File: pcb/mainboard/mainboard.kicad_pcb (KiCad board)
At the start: 10 copper layers, 165 x 121 mm, 629 parts, among them J1 CONN_PCIE_PWR_8PIN, J10 FAN_01, J11 XILINX_JTAG, J12 JUMPER_0402_SPDT, J13 JUMPER_0402_SPDT, J14 RJ45, J15 PMOD_HOST, J16 SMPM, J17 SMPM, J18 SMPM, J19 SMPM, J2 CONN_IBC_MGMT, J20 SMPM, J21 SMPM, J22 SMPM, J23 SMPM, J24 SMPM, J25 SMPM, J26 SMPM, J27 0826-1G1T-23-F, J28 SMPM, J29 SMPM, J3 CONN_01X03, J30 SMPM, J31 SMPM, J32 SMPM, J33 SMPM, J34 SMPM, J35 SMPM, J36 SMPM, J37 SMPM, J38 SMPM, J39 SMPM, J4 CONN_01X05, J40 SMPM, J41 SMPM, J42 SMPM, J43 SMPM, J44 SMPM, J45 SMPM, J46 SMPM, J47 SMPM, J48 CONN_01X10, J5 XILINX_JTAG, J6 CONN_SFP_HOST, J7 SFP_CAGE, J8 FAN_01, J9 CONN_01X03, K1 RELAY_TE_HF3_96, K2 RELAY_TE_HF3_96, K3 RELAY_TE_HF3_96, K4 RELAY_TE_HF3_96, M1 960-23-23-F-AB-0, SW1 SWITCH, SW2 SWITCH, U1 STM32L031C6U6, U10 MAX40026, U11 MAX40026, U12 MAX40026, U13 MAX40026, U14 MAX40026, U15 MAX40026, U16 MAX40026, U17 MAX40026, U18 MAX40026, U19 MAX40026, U2 MYMGK1R812ERSR, U20 MAX40026, U21 DAC60508, U22 DAC60508, U23 STM32H735-UFBGA176-25, U24 AT24MAC402, U25 ADM3101E_QFN, U26 LMR70503, U27 SIT9121AI-2BF-XXS200.000000G, U28 SIT9121AI-2BF-XXS156.250000G, U29 HMC675LP3E, U3 MYMGK00504ERSR, U30 SIT9121AI-2BF-XXS200.000000G, U31 ECS-1612MV-250-CN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

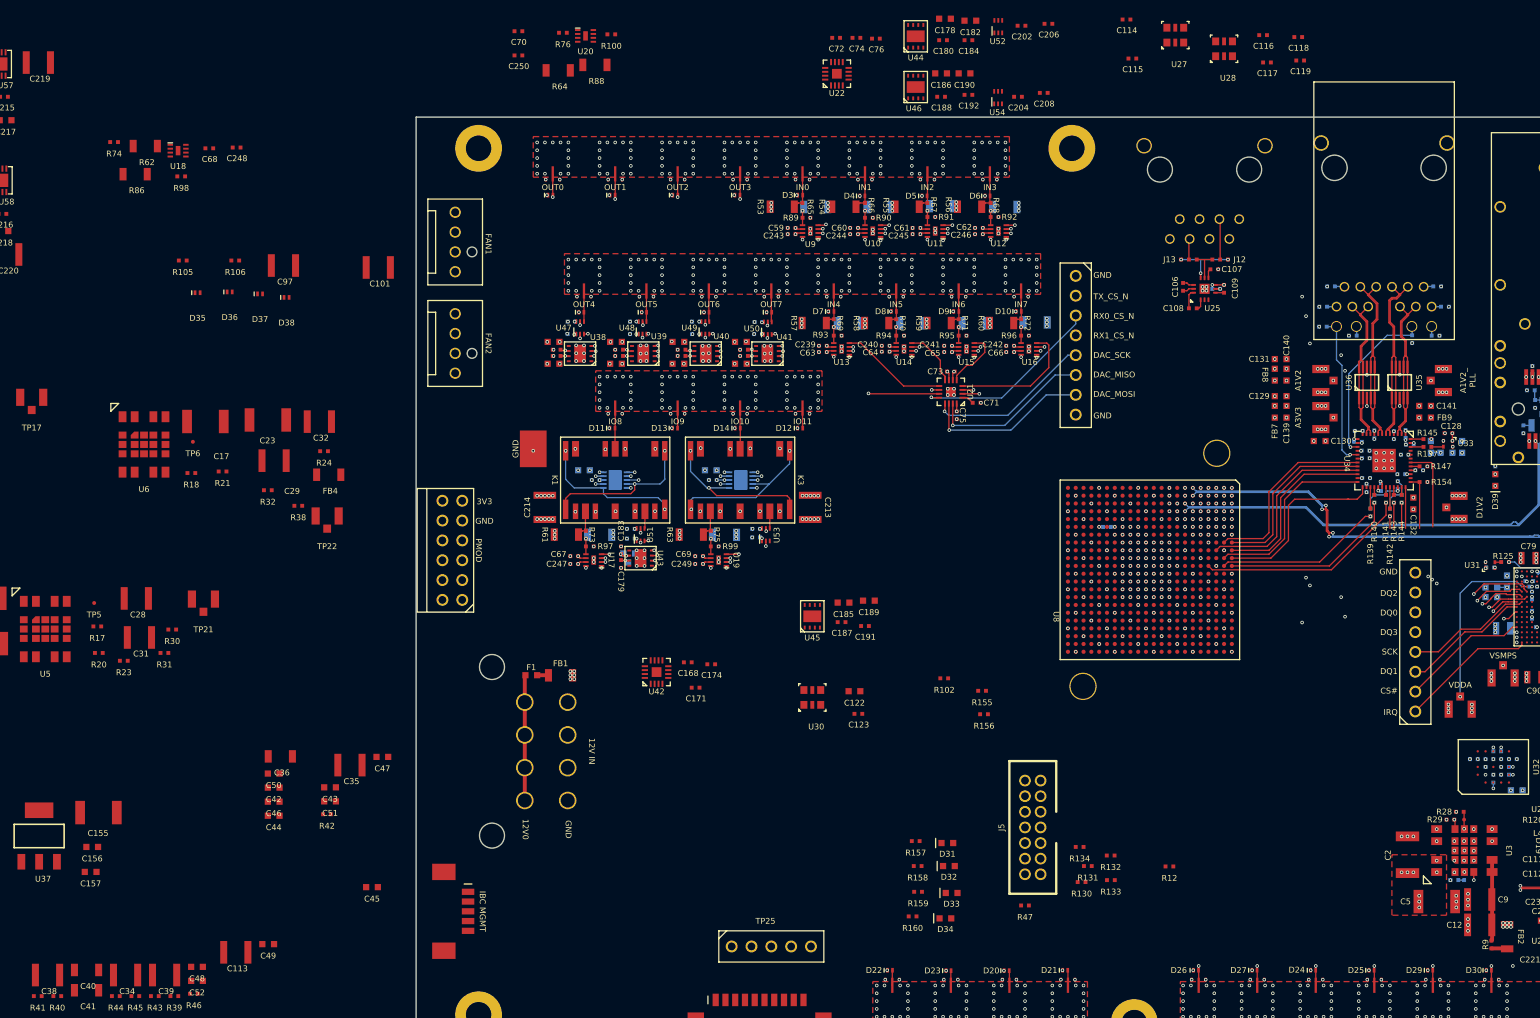
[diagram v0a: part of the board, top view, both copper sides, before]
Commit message: Hooked up most input pins
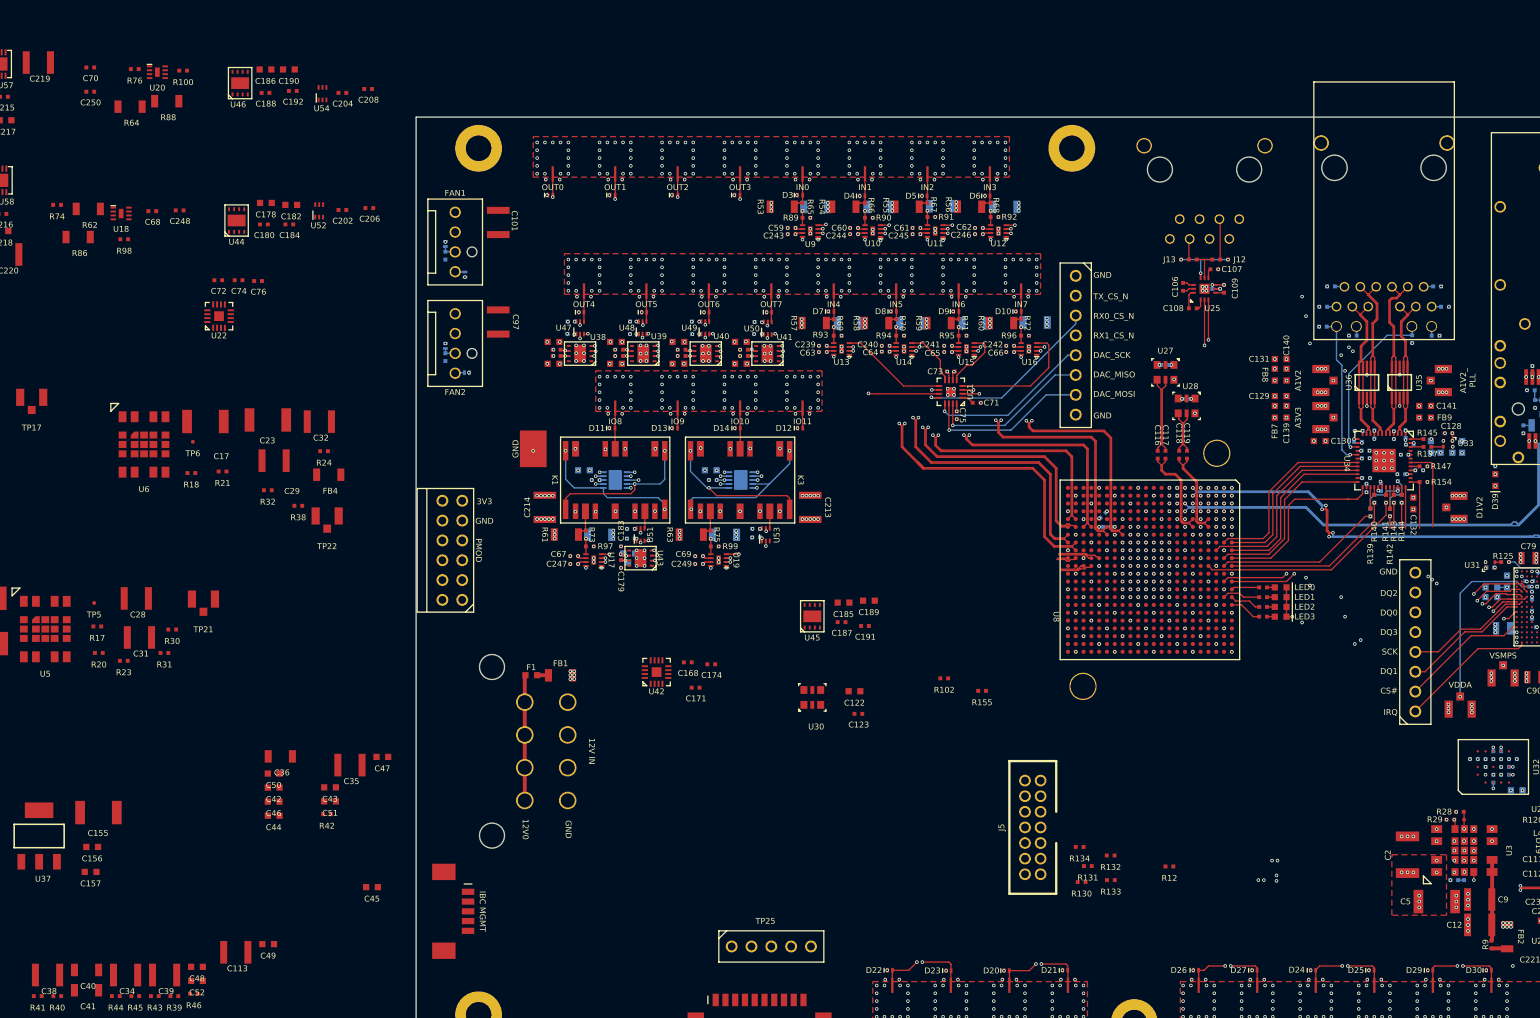
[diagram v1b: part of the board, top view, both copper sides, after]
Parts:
- C114, C115, D35, D36, D37, D38, R105, R106, R156, R47: moved to B.Cu
- moved C202 90.1 mm to (105.5, 31.9)
- moved C178 90.1 mm to (95.8, 31.0)
- moved C180 90.1 mm to (95.5, 33.8)
- moved C182 90.1 mm to (99.0, 31.2)
- moved C184 90.1 mm to (98.8, 33.8)
- moved C206 90.1 mm to (109.0, 31.6)
- moved U44 90.1 mm to (92.0, 33.2)
- moved U52 90.1 mm to (102.6, 32.0)
- moved C208 86.6 mm to (108.8, 16.4)
- moved U54 86.6 mm to (103.0, 17.0)
- moved C186 86.6 mm to (95.7, 13.9)
- moved C188 86.6 mm to (95.7, 16.9)
- moved C190 86.6 mm to (98.7, 13.9)
- moved C192 86.6 mm to (99.2, 16.6)
- moved C204 86.6 mm to (105.5, 16.9)
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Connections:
- R157 pad 1: /Management/FPGA_LED0 -> /FPGA Support/FPGA_LED0
- R158 pad 1: /Management/FPGA_LED1 -> /FPGA Support/FPGA_LED1
- R159 pad 1: /Management/FPGA_LED2 -> /FPGA Support/FPGA_LED2
- R160 pad 1: /Management/FPGA_LED3 -> /FPGA Support/FPGA_LED3
- R163 pad 1: /Management/SFP_LED1 -> /FPGA Support/SFP_LED1
- R164 pad 1: /Management/SFP_LED2 -> /FPGA Support/SFP_LED2
- U8 pad A13: unconnected-(U8-PadA13) -> /FPGA Support/SFP_LED1
- U8 pad A14: unconnected-(U8-PadA14) -> /FPGA Support/FPGA_LED0
- U8 pad A15: unconnected-(U8-PadA15) -> /FPGA Support/FPGA_LED2
- U8 pad A16: unconnected-(U8-PadA16) -> /FPGA Support/FPGA_LED3
- U8 pad A3: /Transceivers/BERT_TX1_N -> /Transceivers/BERT_TX0_N
- U8 pad A4: /Transceivers/BERT_TX1_P -> /Transceivers/BERT_TX0_P
- U8 pad AA10: /Inputs/TRIGIN_3_P -> /Inputs/TRIGIN_9_P
- U8 pad AA5: /Inputs/TRIGIN_0_P -> /Inputs/TRIGIN_2_N
- U8 pad AA6: /Inputs/TRIGIN_2_P -> /Inputs/TRIGIN_5_N
- U8 pad AB10: /Inputs/TRIGIN_3_N -> /Inputs/TRIGIN_9_N
- U8 pad AB5: /Inputs/TRIGIN_0_N -> /Inputs/TRIGIN_2_P
- U8 pad AB6: /Inputs/TRIGIN_2_N -> /Inputs/TRIGIN_5_P
- U8 pad B1: /Transceivers/BERT_TX0_N -> /Transceivers/BERT_TX1_N
- U8 pad B13: unconnected-(U8-PadB13) -> /FPGA Support/SFP_LED2
- U8 pad B15: unconnected-(U8-PadB15) -> /FPGA Support/FPGA_LED1
- U8 pad B2: /Transceivers/BERT_TX0_P -> /Transceivers/BERT_TX1_P
- U8 pad B5: /Transceivers/BERT_RX1_N -> /Transceivers/BERT_RX0_N
- U8 pad B6: /Transceivers/BERT_RX1_P -> /Transceivers/BERT_RX0_P
- U8 pad C3: /Transceivers/BERT_RX0_N -> /Transceivers/BERT_RX1_N
- U8 pad C4: /Transceivers/BERT_RX0_P -> /Transceivers/BERT_RX1_P
- U8 pad F20: /Management/FPGA_LED1 -> unconnected-(U8-PadF20)
- U8 pad G20: /Management/FPGA_LED0 -> unconnected-(U8-PadG20)
- U8 pad K19: /Management/FPGA_LED3 -> unconnected-(U8-PadK19)
- U8 pad L18: /Management/FPGA_LED2 -> unconnected-(U8-PadL18)
- U8 pad L19: /Management/SFP_LED1 -> unconnected-(U8-PadL19)
- U8 pad L20: /Management/SFP_LED2 -> unconnected-(U8-PadL20)
- U8 pad U6: /Inputs/TRIGIN_9_N -> /Inputs/TRIGIN_3_N
- U8 pad U7: /Inputs/TRIGIN_9_P -> /Inputs/TRIGIN_3_P
- U8 pad W11: /Inputs/TRIGIN_5_P -> /Inputs/TRIGIN_0_P
- U8 pad W6: /Inputs/TRIGIN_6_P -> /Inputs/TRIGIN_6_N
- U8 pad Y11: /Inputs/TRIGIN_5_N -> /Inputs/TRIGIN_0_N
- U8 pad Y6: /Inputs/TRIGIN_6_N -> /Inputs/TRIGIN_6_P
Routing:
- net /Transceivers/BERT_TX0_N: track 1.90 -> 109.7 mm, vias 1 -> 3
- net /Transceivers/BERT_TX0_P: track 1.95 -> 108.4 mm, vias 1 -> 3
- net /Transceivers/BERT_TX1_N: track 1.95 -> 101.0 mm, vias 1 -> 3
- net /Transceivers/BERT_TX1_P: track 1.90 -> 100.3 mm, vias 1 -> 3
- net /Transceivers/FASTSYNC_TX_N: track 2.47 -> 95.2 mm
- net /Transceivers/FASTSYNC_TX_P: track 2.49 -> 95.2 mm
- net /Transceivers/BERT_RX1_N: track 2.51 -> 76.5 mm
- net /Transceivers/BERT_RX1_P: track 2.50 -> 76.2 mm
- net /Management/MCU_UART_RX: track 25.6 -> 93.4 mm, vias 1 -> 4
- net /Management/MCU_UART_TX: track 26.5 -> 93.8 mm, vias 1 -> 4
- net /Transceivers/BERT_RX0_P: track 2.51 -> 66.2 mm
- net /Transceivers/BERT_RX0_N: track 2.61 -> 66.3 mm
- net /GND: track 1866.9 -> 1924.6 mm, vias 1149 -> 1156
- net /Transceivers/CDRTRIG_RX_N: track 43.4 -> 99.3 mm, vias 2 -> 3
- net /Transceivers/CDRTRIG_RX_P: track 43.2 -> 99.0 mm, vias 2 -> 3
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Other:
- board text removed: "FPGA LEDs"
- board text removed: "GTX clocks"

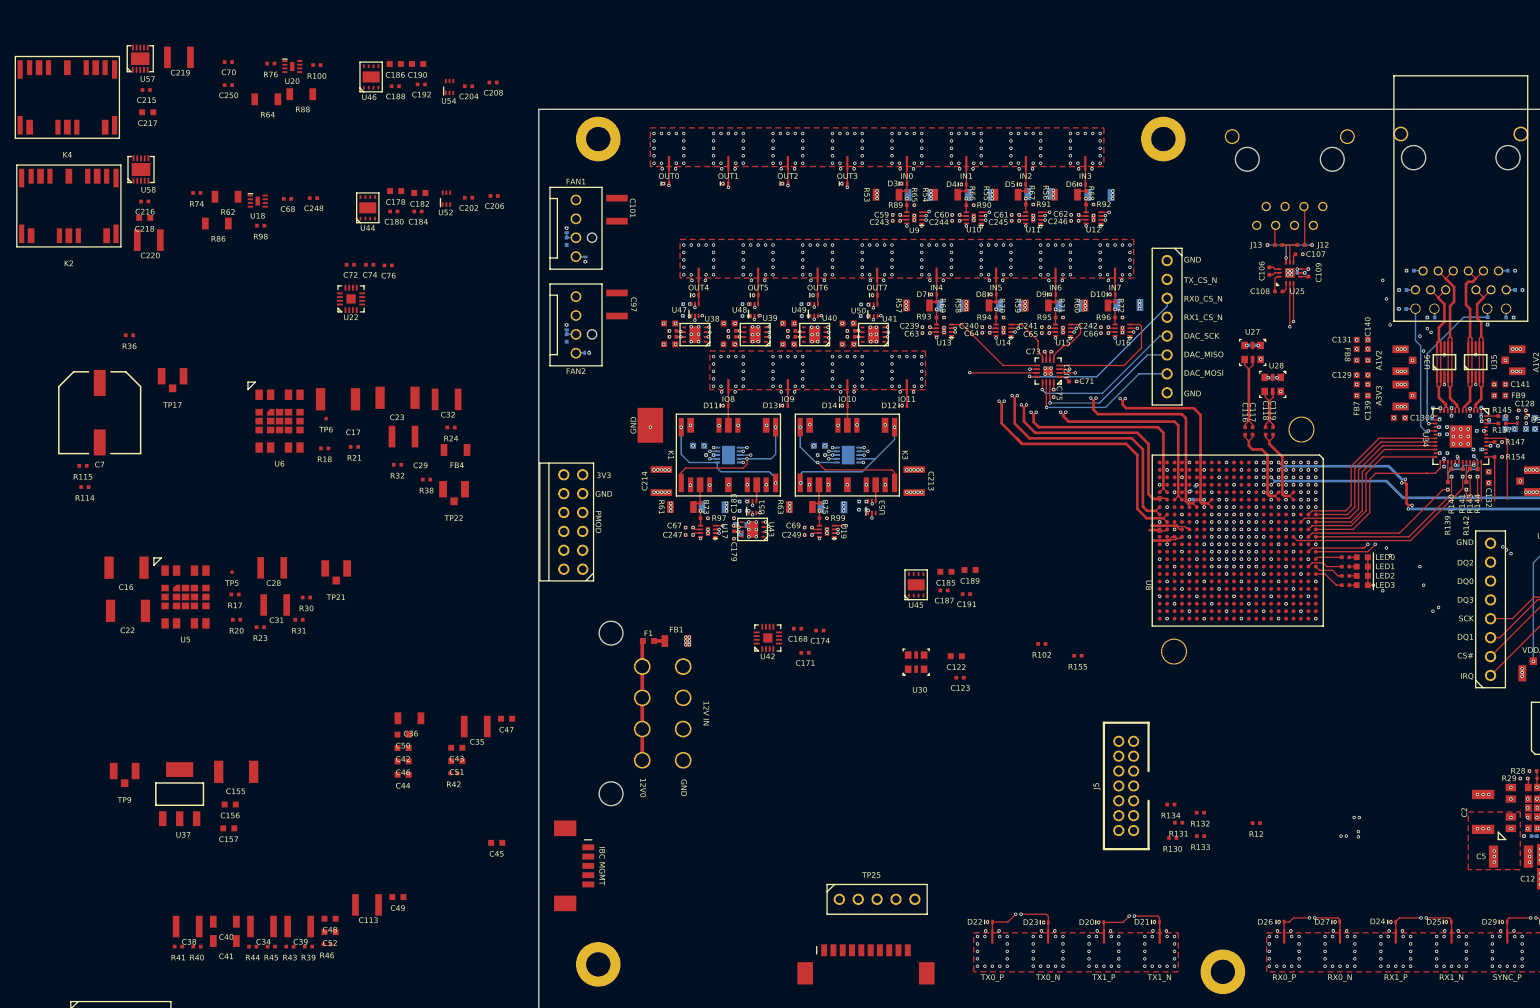
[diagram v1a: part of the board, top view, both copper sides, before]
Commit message: Hooked up PMOD, initial placement of FPGA JTAG
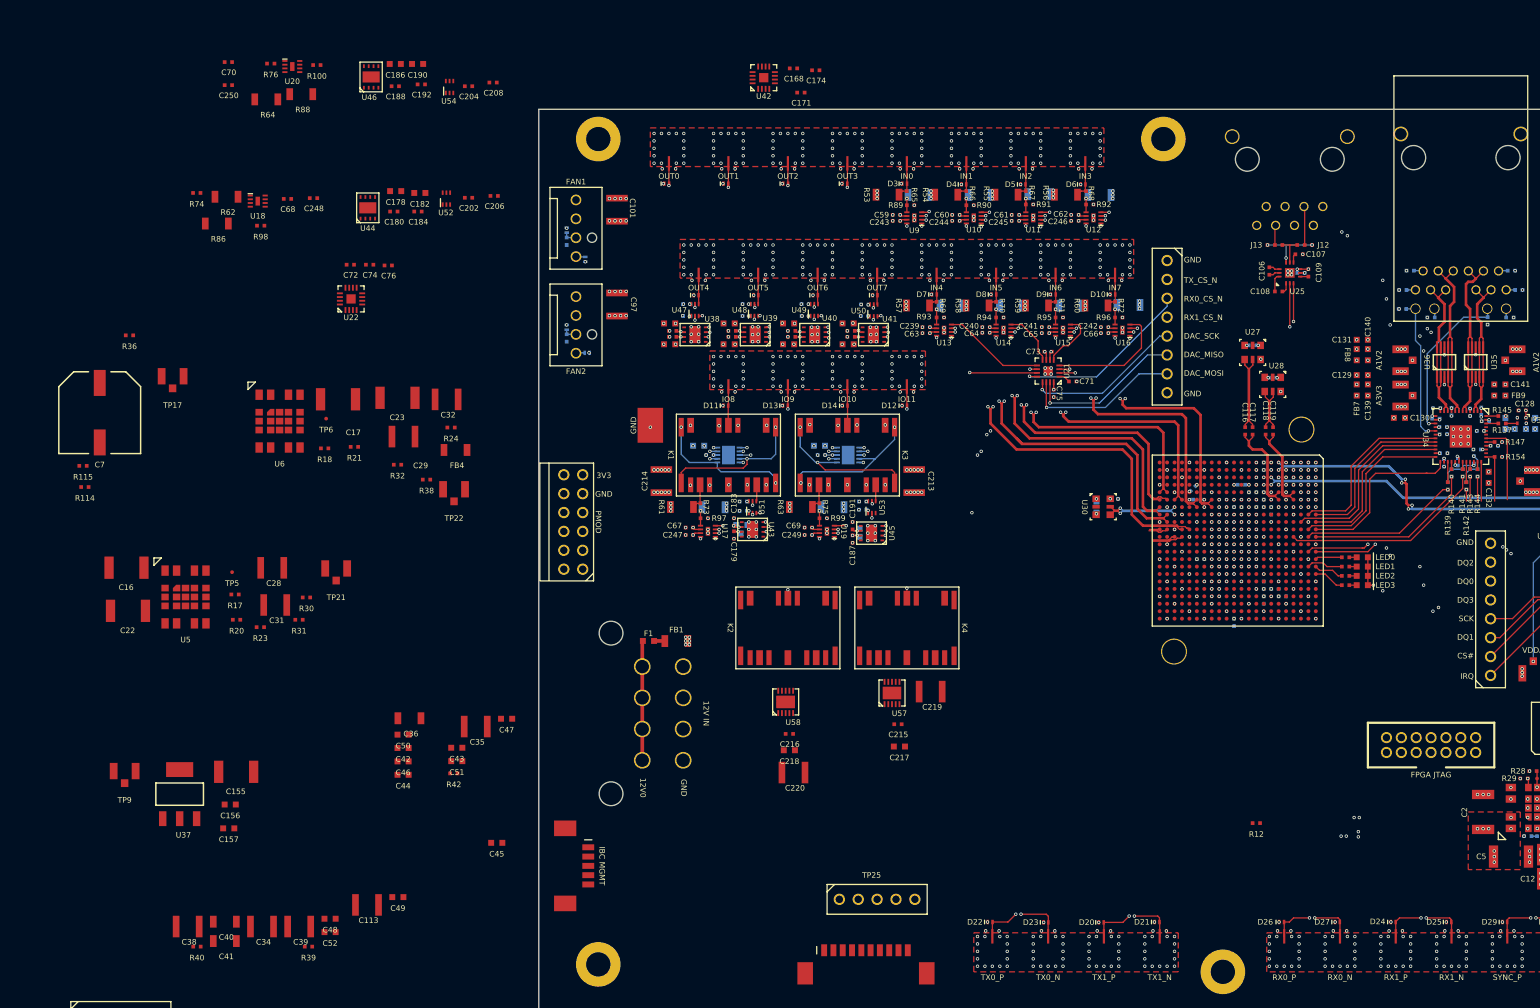
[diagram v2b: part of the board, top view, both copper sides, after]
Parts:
- C122, C123, C185, C189, R102, R130, R131, R132, R133, R134, R155, R41, R43, R44, R45, R46: moved to B.Cu
- moved R41 154.3 mm to (209.0, 73.5)
- moved R44 147.8 mm to (212.0, 73.5)
- moved R45 146.6 mm to (212.5, 72.0), turned to -90 degrees
- moved R43 144.4 mm to (213.5, 74.0), turned to 90 degrees
- moved R46 138.5 mm to (211.0, 71.5)
- moved K4 133.6 mm to (164.5, 89.8), turned to 180 degrees
- moved C215 132.3 mm to (163.3, 102.7)
- moved C217 132.3 mm to (163.5, 105.7)
- moved C219 132.3 mm to (167.7, 98.3)
- moved U57 132.3 mm to (162.5, 98.5)
- moved C216 112.4 mm to (148.7, 104.0)
- moved C218 112.4 mm to (148.7, 106.2)
- moved C220 112.4 mm to (149.2, 109.2)
- moved U58 112.4 mm to (148.2, 99.7)
- moved K2 112.1 mm to (148.5, 89.8), turned to 180 degrees
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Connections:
- U8 pad G21: unconnected-(U8-PadG21) -> /Management/SFP_RX_LOS
- U8 pad J19: /Management/SFP_RX_LOS -> unconnected-(U8-PadJ19)
- U8 pad K21: unconnected-(U8-PadK21) -> /Management/MCU_QSPI_SCK
- U8 pad K22: unconnected-(U8-PadK22) -> /Management/MCU_QSPI_DQ2
- U8 pad L20: unconnected-(U8-PadL20) -> /Management/MCU_QSPI_DQ0
- U8 pad M16: /Management/PMOD_DQ7 -> /Management/PMOD_DQ3
- U8 pad M21: unconnected-(U8-PadM21) -> /Management/MCU_QSPI_CS_N
- U8 pad N17: /Management/PMOD_DQ4 -> /Management/PMOD_DQ7
- U8 pad N22: unconnected-(U8-PadN22) -> /Management/MCU_QSPI_DQ1
- U8 pad P16: /Management/PMOD_DQ3 -> /Management/PMOD_DQ2
- U8 pad P17: /Management/PMOD_DQ0 -> /Management/PMOD_DQ6
- U8 pad P19: /Management/MCU_QSPI_DQ0 -> /Management/PMOD_DQ4
- U8 pad P20: /Management/MCU_QSPI_SCK -> unconnected-(U8-PadP20)
- U8 pad P21: /Management/PMOD_DQ1 -> unconnected-(U8-PadP21)
- U8 pad P22: /Management/PMOD_DQ2 -> unconnected-(U8-PadP22)
- U8 pad R17: /Management/MCU_QSPI_CS_N -> /Management/PMOD_DQ1
- U8 pad R18: /Management/MCU_QSPI_DQ2 -> /Management/PMOD_DQ5
- U8 pad R19: /Management/MCU_QSPI_DQ1 -> /Management/PMOD_DQ0
- U8 pad R21: /Management/PMOD_DQ5 -> unconnected-(U8-PadR21)
- U8 pad R22: /Management/PMOD_DQ6 -> unconnected-(U8-PadR22)
- U8 pad V10: /Inputs/TRIGIN_10_P -> /Inputs/TRIGIN_0_N
- U8 pad W10: /Inputs/TRIGIN_10_N -> /Inputs/TRIGIN_0_P
- U8 pad W11: /Inputs/TRIGIN_0_P -> /Inputs/TRIGIN_10_P
- U8 pad Y11: /Inputs/TRIGIN_0_N -> /Inputs/TRIGIN_10_N
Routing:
- net /Management/FAN1_PWM: track 112.0 -> 164.8 mm, vias 1 -> 2
- net /Management/FAN1_TACH: track 80.2 -> 132.2 mm, vias 0 -> 1
- net /Management/PMOD_DQ3: track 41.8 -> 92.8 mm, vias 0 -> 1
- net /GND: track 1924.6 -> 1975.1 mm, vias 1156 -> 1175
- net /Management/PMOD_DQ7: track 44.5 -> 94.6 mm, vias 0 -> 1
- net /Management/PMOD_DQ4: track 42.9 -> 90.1 mm, vias 0 -> 1
- net /Management/PMOD_DQ2: track 41.4 -> 88.4 mm, vias 0 -> 1
- net /Management/PMOD_DQ6: track 44.1 -> 90.9 mm, vias 0 -> 1
- net /Management/PMOD_DQ0: track 40.0 -> 86.1 mm, vias 0 -> 1
- net /Management/PMOD_DQ5: track 43.5 -> 89.3 mm, vias 0 -> 1
- net /Management/PMOD_DQ1: track 41.0 -> 86.3 mm, vias 0 -> 1
- net /Inputs/TRIGIN_0_N: track 29.1 -> 70.4 mm, vias 1 -> 2
- net /Inputs/TRIGIN_0_P: track 30.2 -> 69.6 mm, vias 1 -> 2
- net /Connectors/OE8B: track 22.4 -> 52.4 mm, vias 1 -> 2
- net /Connectors/OE8A: track 21.9 -> 51.6 mm, vias 1 -> 2
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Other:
- board text added: "FPGA JTAG"
